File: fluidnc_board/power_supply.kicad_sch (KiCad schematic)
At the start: 55 parts

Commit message: footprint associations and part no.
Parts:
- added C70, C72, C83: 100n, Capacitor_SMD:C_0603_1608Metric_Pad1.05x0.95mm_HandSolder, symbol Device:C
- C76, C77, C85: renamed from C?; Digikey Part No. 1276-CL05B682KB5VPNCCT-ND -> 1276-1586-1-ND
- C81: renamed from C?; footprint Capacitor_THT:CP_Radial_D8.0mm_P3.50mm -> Capacitor_SMD:CP_Elec_10x10; Digikey Part No. 399-6119-ND -> UCD1H101MCL6CT-ND
- C82, C89: renamed from C?; value 1u -> 4.7u; footprint Capacitor_SMD:C_1206_3216Metric_Pad1.33x1.80mm_HandSolder -> Capacitor_SMD:C_0805_2012Metric_Pad1.18x1.45mm_HandSolder; Digikey Part No. 1276-1204-1-ND -> 1276-1248-1-ND
- C84, C88: renamed from C?; footprint (none) -> Capacitor_SMD:C_0603_1608Metric_Pad1.05x0.95mm_HandSolder; Digikey Part No. (none) -> 1276-1941-1-ND
- C87: renamed from C?; value 22u -> 4.7u; footprint (none) -> Capacitor_SMD:C_0805_2012Metric_Pad1.18x1.45mm_HandSolder; Digikey Part No. (none) -> 1276-1248-1-ND
- D50, D51: renamed from D?; Digikey Part No. 404-1046-1-ND -> 160-1457-1-ND
- R52, R54, R57, R58, R64, R66: renamed from R?; footprint Resistor_SMD:R_0805_2012Metric_Pad1.15x1.40mm_HandSolder -> Resistor_SMD:R_0805_2012Metric_Pad1.20x1.40mm_HandSolder
- R59: renamed from R?; Digikey Part No. 311-2.2KGRCT-ND -> 311-2.20KHRCT-ND
- R60: renamed from R?; Digikey Part No. 311-200GRCT-ND -> 311-200HRCT-ND
- R61: renamed from R?; footprint Resistor_SMD:R_0805_2012Metric_Pad1.15x1.40mm_HandSolder -> Resistor_SMD:R_0603_1608Metric_Pad0.98x0.95mm_HandSolder; Digikey Part No. 311-12KARCT-ND -> 311-3.00KHRCT-ND
- R62: renamed from R?; footprint Resistor_SMD:R_0805_2012Metric_Pad1.15x1.40mm_HandSolder -> Resistor_SMD:R_0603_1608Metric_Pad0.98x0.95mm_HandSolder; Digikey Part No. YAG6172CT-ND -> 311-750HRCT-ND
- R67: renamed from R?; footprint Resistor_SMD:R_0805_2012Metric_Pad1.15x1.40mm_HandSolder -> Resistor_SMD:R_0603_1608Metric_Pad0.98x0.95mm_HandSolder; Digikey Part No. 311-12KARCT-ND -> 311-12.0KHRCT-ND
- R68, R69, R70: renamed from R?; Digikey Part No. YAG6172CT-ND -> 311-.27LUCT-ND
- R71: renamed from R?; footprint Resistor_SMD:R_0805_2012Metric_Pad1.15x1.40mm_HandSolder -> Resistor_SMD:R_0603_1608Metric_Pad0.98x0.95mm_HandSolder; Digikey Part No. YAG6172CT-ND -> 311-100GRCT-ND
- U26: renamed from U?; footprint (none) -> Package_TO_SOT_SMD:SOT-89-3; Digikey Part No. (none) -> AZ1117CR-3.3TRG1DICT-ND
- gave numbers to parts that had none: 28
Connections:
- net 48VDC: now also C70.1, C72.1, C83.1
- net GND: now also C70.2, C72.2, C83.2

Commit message: fixed some footprint associations, placed footprints
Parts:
- C70, C72, C78, C79, C80, C83, C84, C86, C88: footprint Capacitor_SMD:C_0603_1608Metric_Pad1.05x0.95mm_HandSolder -> Capacitor_SMD:C_0603_1608Metric_Pad1.08x0.95mm_HandSolder; Digikey Part No. 1276-1941-1-ND -> (none)
- C76, C77, C85: Digikey Part No. 1276-1586-1-ND -> (none)
- C82, C87, C89: Digikey Part No. 1276-1248-1-ND -> (none)
- D47, D48, D49: Digikey Part No. SS2150-LTPMSCT-ND -> (none)
- D50, D51: Digikey Part No. 160-1457-1-ND -> (none)
- F1, F3: Digikey Part No. 118-MF-RHT200/32-0-ND -> (none)
- F2: footprint Fuse:Fuse_1812_4532Metric_Castellated -> Fuse:Fuse_1206_3216Metric_Pad1.42x1.75mm_HandSolder; Digikey Part No. 507-1758-1-ND -> (none)
- J20: Digikey Part No. ED2810-ND -> (none)
- L1: Digikey Part No. 732-1140-1-ND -> (none)
- L2, L3, L4: Digikey Part No. 541-2273-1-ND -> (none)
- R51, R53, R63: Digikey Part No. 311-100KGRCT-ND -> (none)
- R52, R54, R57, R58, R64, R66: Digikey Part No. 311-10KARCT-ND -> (none)
- R55, R56, R65: footprint Resistor_SMD:R_0805_2012Metric_Pad1.15x1.40mm_HandSolder -> Resistor_SMD:R_0805_2012Metric_Pad1.20x1.40mm_HandSolder; Digikey Part No. 311-47KARCT-ND -> (none)
- R59: Digikey Part No. 311-2.20KHRCT-ND -> (none)
- R60: Digikey Part No. 311-200HRCT-ND -> (none)
- R61: Digikey Part No. 311-3.00KHRCT-ND -> (none)
- R62: Digikey Part No. 311-750HRCT-ND -> (none)
- R67: Digikey Part No. 311-12.0KHRCT-ND -> (none)
- R68, R69, R70: footprint Resistor_SMD:R_0805_2012Metric_Pad1.15x1.40mm_HandSolder -> Resistor_SMD:R_1206_3216Metric_Pad1.30x1.75mm_HandSolder; Digikey Part No. 311-.27LUCT-ND -> (none)
- R71: footprint Resistor_SMD:R_0603_1608Metric_Pad0.98x0.95mm_HandSolder -> Resistor_SMD:R_1206_3216Metric_Pad1.30x1.75mm_HandSolder; Digikey Part No. 311-100GRCT-ND -> (none)
- U23, U24, U25: Digikey Part No. BD9G341AEFJ-E2CT-ND -> (none)
- U26: Digikey Part No. AZ1117CR-3.3TRG1DICT-ND -> (none)

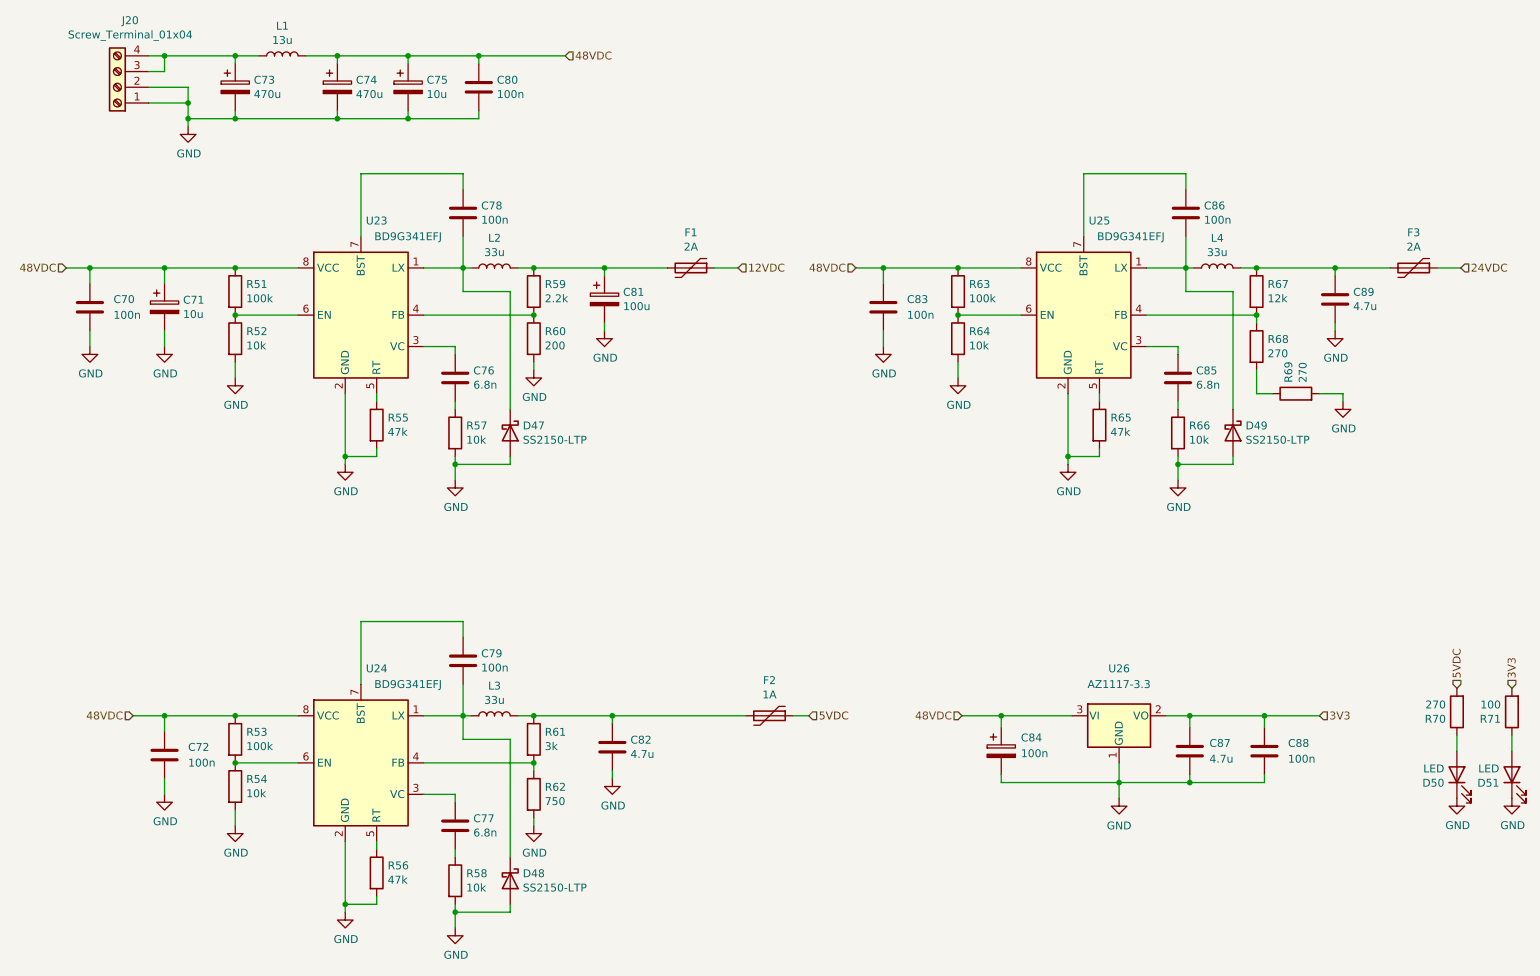
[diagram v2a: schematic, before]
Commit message: placed and routed one stepper motor unit
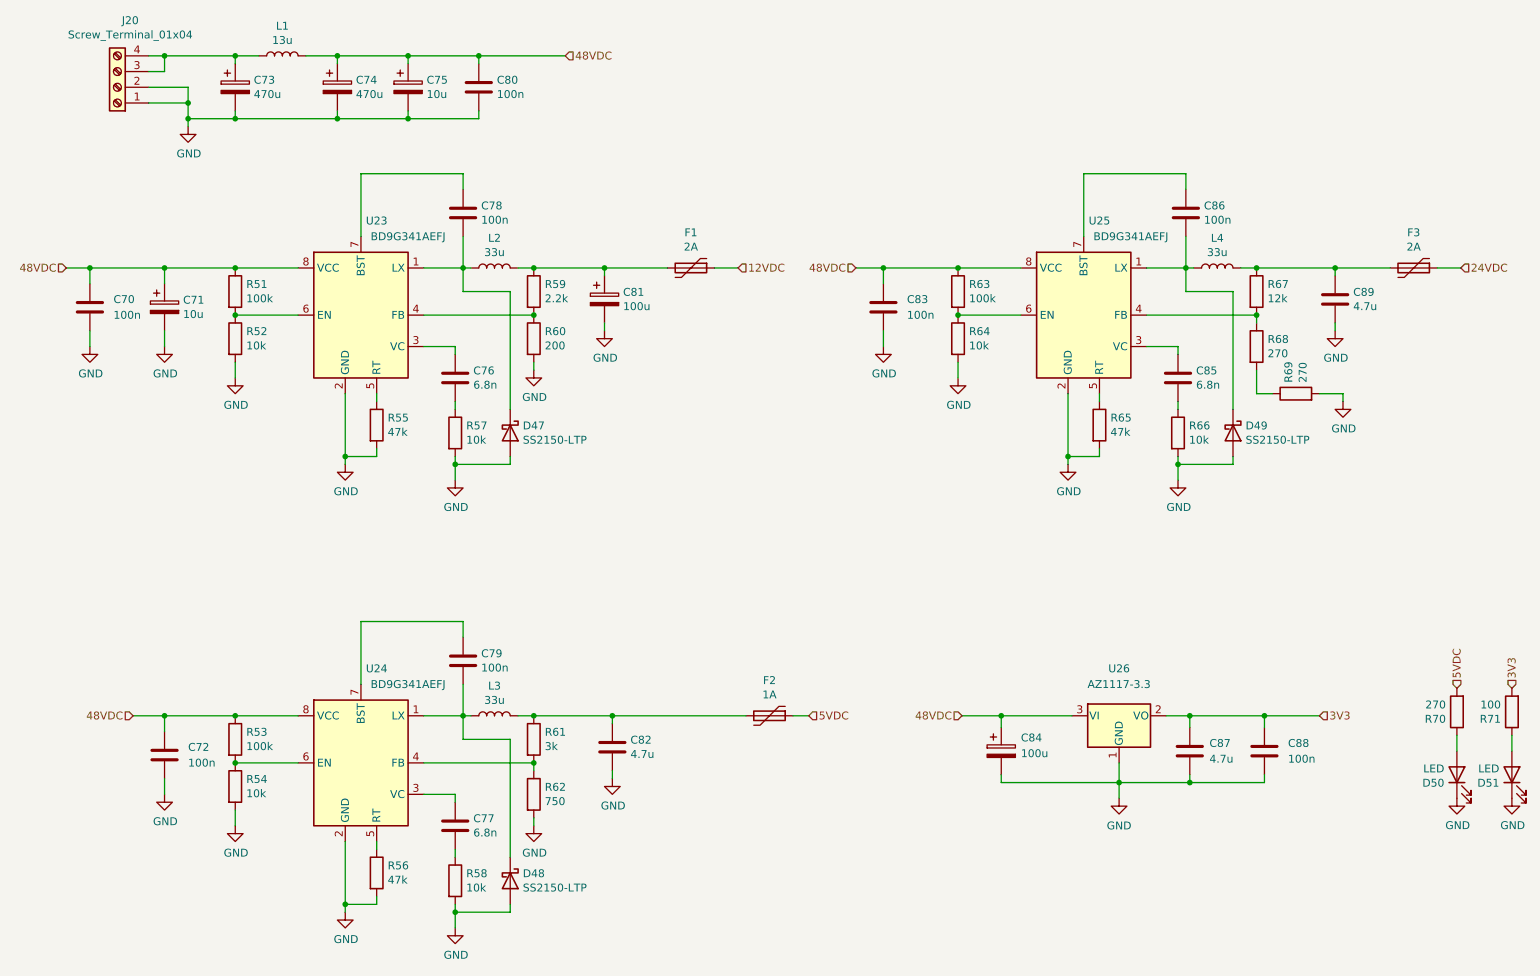
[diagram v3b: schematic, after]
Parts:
- C84: value 100n -> 100u; footprint Capacitor_SMD:C_0603_1608Metric_Pad1.08x0.95mm_HandSolder -> Capacitor_SMD:CP_Elec_10x10
- U23, U24, U25: value BD9G341EFJ -> BD9G341AEFJ; symbol Regulator_Switching:BD9G341EFJ -> fluidnc_board:BD9G341AEFJ
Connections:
- net GND: now also U23.9 (GND), U24.9 (GND), U25.9 (GND)
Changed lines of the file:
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@@
       (effects (font (size 1.27 1.27)) (justify left))
     )
-    (property "Value" "100n" (id 1) (at 186.69 139.4459 0)
-      (effects (font (size 1.27 1.27)) (justify left))
-    )
-    (property "Footprint" "Capacitor_SMD:C_0603_1608Metric_Pad1.08x0.95mm_HandSolder" (id 2) (at 184.4802 142.875 0)
-      (effects (font (size 1.27 1.27)) hide)
-    )
-    (property "Datasheet" "~" (id 3) (at 183.515 139.065 0)
+    (property "Value" "100u" (id 1) (at 186.69 139.4459 0)
+      (effects (font (size 1.27 1.27)) (justify left))
+    )
+    (property "Footprint" "Capacitor_SMD:CP_Elec_10x10" (id 2) (at 184.4802 142.875 0)
+      (effects (font (size 1.27 1.27)) hide)
+    )
+    (property "Datasheet" "https://www.nichicon.co.jp/english/products/pdfs/e-ucd.pdf" (id 3) (at 183.515 139.065 0)
       (effects (font (size 1.27 1.27)) hide)
     )
@@
     (pin "1")
   )
-  (symbol (lib_id "Regulator_Switching:BD9G341EFJ") (at 80.01 68.58 0) (unit 1)
+  (symbol (lib_id "fluidnc_board:BD9G341AEFJ") (at 80.01 68.58 0) (unit 1)
     (in_bom yes) (on_board yes)
     (property "Reference" "U23" (id 0) (at 82.55 53.34 0))
-    (property "Value" "BD9G341EFJ" (id 1) (at 87.63 55.88 0))
+    (property "Value" "BD9G341AEFJ" (id 1) (at 87.63 55.88 0))
     (property "Footprint" "Package_SO:HTSOP-8-1EP_3.9x4.9mm_P1.27mm_EP2.4x3.2mm_ThermalVias" (id 2) (at 82.55 80.01 0)
       (effects (font (size 1.27 1.27)) (justify left) hide)
@@
       (effects (font (size 1.27 1.27)) hide)
     )
+    (pin "9")
     (pin "1")
     (pin "2")
@@
     (pin "2")
   )
-  (symbol (lib_id "Regulator_Switching:BD9G341EFJ") (at 196.85 68.58 0) (unit 1)
+  (symbol (lib_id "fluidnc_board:BD9G341AEFJ") (at 196.85 68.58 0) (unit 1)
     (in_bom yes) (on_board yes)
     (property "Reference" "U25" (id 0) (at 199.39 53.34 0))
-    (property "Value" "BD9G341EFJ" (id 1) (at 204.47 55.88 0))
+    (property "Value" "BD9G341AEFJ" (id 1) (at 204.47 55.88 0))
     (property "Footprint" "Package_SO:HTSOP-8-1EP_3.9x4.9mm_P1.27mm_EP2.4x3.2mm_ThermalVias" (id 2) (at 199.39 80.01 0)
       (effects (font (size 1.27 1.27)) (justify left) hide)
@@
       (effects (font (size 1.27 1.27)) hide)
     )
+    (pin "9")
     (pin "1")
     (pin "2")
@@
     (pin "2")
   )
-  (symbol (lib_id "Regulator_Switching:BD9G341EFJ") (at 80.01 140.97 0) (unit 1)
+  (symbol (lib_id "fluidnc_board:BD9G341AEFJ") (at 80.01 140.97 0) (unit 1)
     (in_bom yes) (on_board yes)
     (property "Reference" "U24" (id 0) (at 82.55 125.73 0))
-    (property "Value" "BD9G341EFJ" (id 1) (at 87.63 128.27 0))
+    (property "Value" "BD9G341AEFJ" (id 1) (at 87.63 128.27 0))
     (property "Footprint" "Package_SO:HTSOP-8-1EP_3.9x4.9mm_P1.27mm_EP2.4x3.2mm_ThermalVias" (id 2) (at 82.55 152.4 0)
       (effects (font (size 1.27 1.27)) (justify left) hide)
@@
       (effects (font (size 1.27 1.27)) hide)
     )
-    (pin "1")
-    (pin "2")
+    (pin "9")
+    (pin "1")
+    (pin "2")
